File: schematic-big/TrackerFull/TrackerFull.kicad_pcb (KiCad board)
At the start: 2 copper layers, 43 x 61 mm, 50 parts, among them J1 SIM_Card, J2 Conn_01x05_Male, J7 Screw_Terminal_01x02, J8 USB_B_Mini, Q1 IRLML5203, Q2 IRLML0030, Q3 IRLML0030, U1 U.FL, U2 LIS3DSH, U3 MCP73831-2-OT, U4 LM350_TO220, U6 ATtiny85-20SU, U7 MCP1700-2502E_SOT23

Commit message: schematic fixes
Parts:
- C4, U7: moved to B.Cu
- R10, R11, R9: value 140 -> 125
- moved Q3 41.3 mm to (125.4, 101.8)
- moved U7 36.4 mm to (109.5, 90.7), turned to 180 degrees
- moved C4 31.8 mm to (106.4, 94.3), turned to 90 degrees
- moved C14 13.8 mm to (94.3, 41.5)
- moved D1 13.8 mm to (95.4, 44.6)
- moved R1 13.8 mm to (94.8, 48.4)
- moved R2 13.8 mm to (93.0, 48.4)
- moved U4 13.8 mm to (90.2, 47.7)
- moved L1 7.12 mm to (119.1, 60.3)
- moved C15 4.16 mm to (117.6, 55.2)
- moved LED1 2.60 mm to (91.4, 87.0)
- moved R10 2.60 mm to (92.0, 81.6)
- moved R11 2.60 mm to (95.5, 88.9)
- moved R9 2.60 mm to (95.5, 84.8)
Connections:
- LED1 pad 4: /VBAT -> /2.2V
- LED1 pad 5: /VBAT -> /2.2V
- LED1 pad 6: /VBAT -> /2.2V
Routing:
- net /2.2V: track 0.00 -> 24.4 mm, vias 0 -> 3
- net /VBAT: track 50.7 -> 34.9 mm

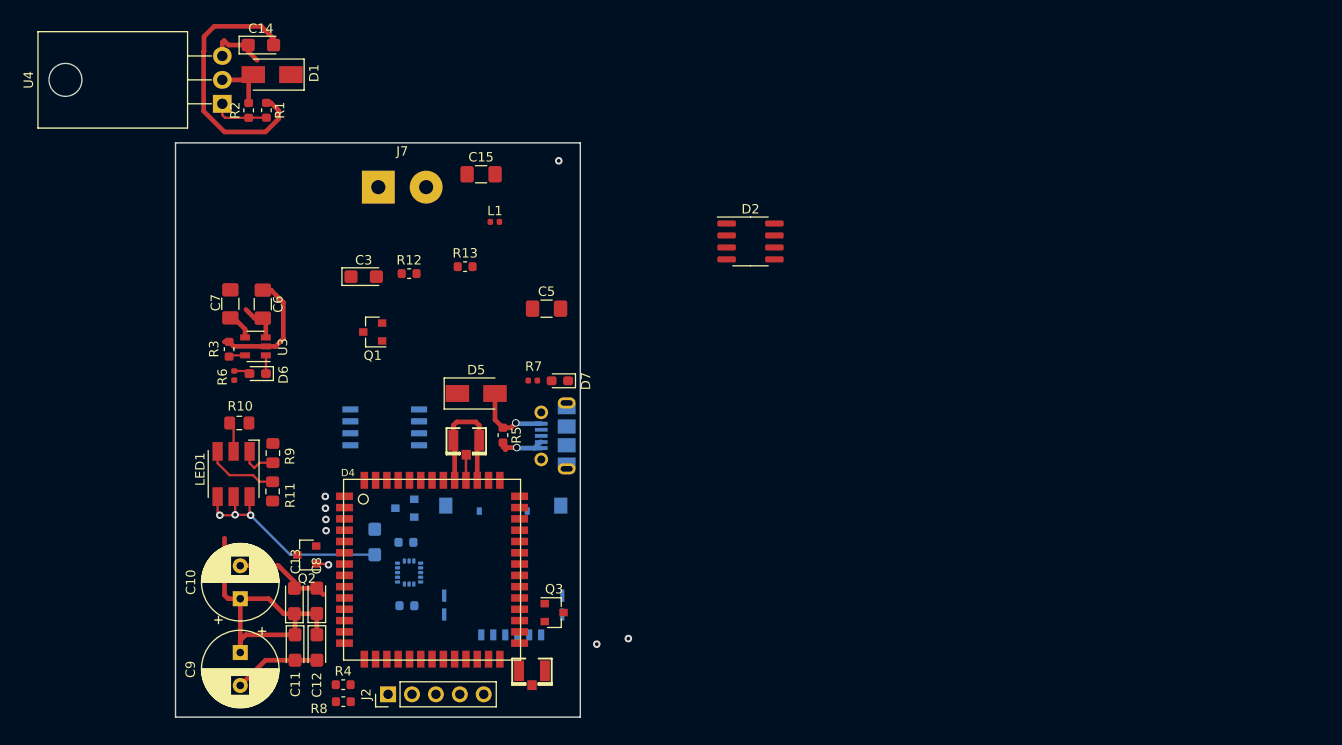
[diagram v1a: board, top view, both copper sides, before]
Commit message: schematic update
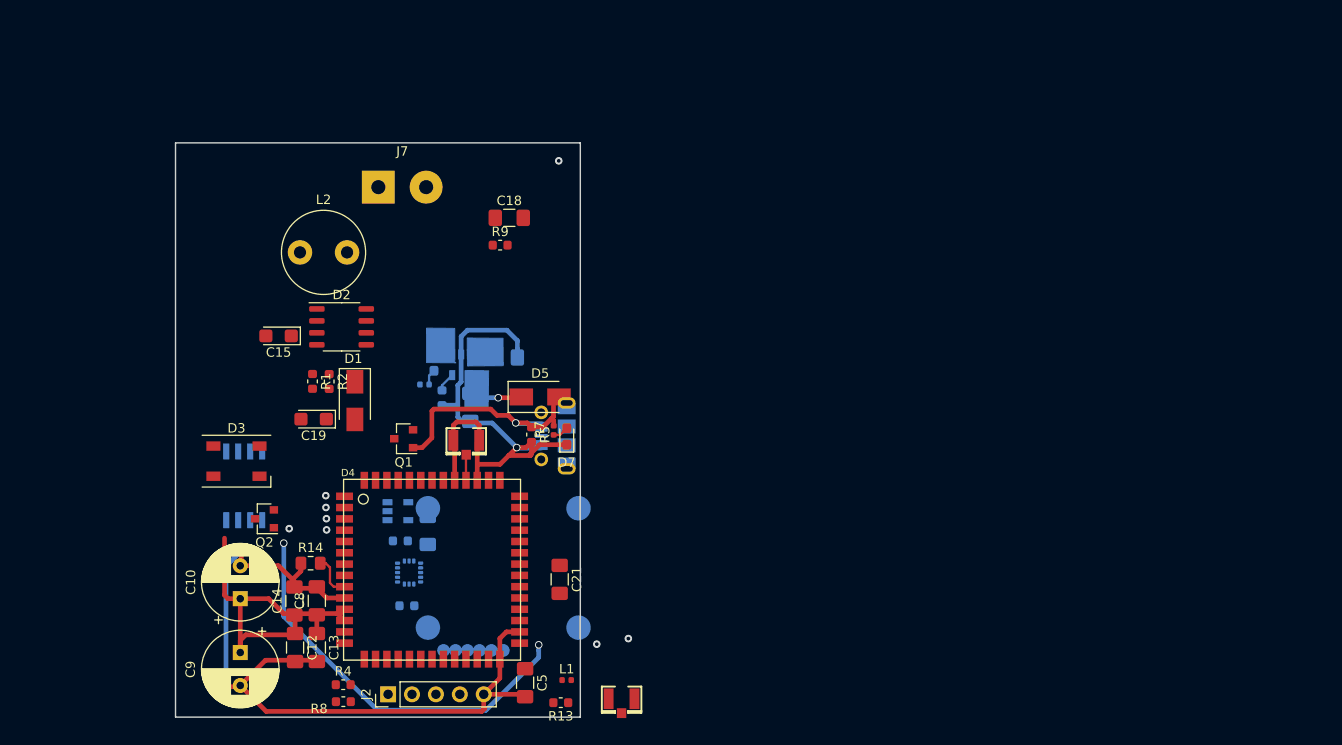
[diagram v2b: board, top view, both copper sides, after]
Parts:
- removed the C14 at (94.3, 41.5)
- removed C3, C4: 10uF, Capacitor_Tantalum_SMD:CP_EIA-3216-18_Kemet-A
- removed LED1: TO-5050BC-MRPBFGF, LED_SMD:LED_RGB_5050-6
- removed Q3: IRLML0030, Package_TO_SOT_SMD:SOT-23
- removed R10, R11: 125, Resistor_SMD:R_0805_2012Metric_Pad1.15x1.40mm_HandSolder
- removed R12: 100K, Resistor_SMD:R_0603_1608Metric
- removed U4: LM350_TO220, Package_TO_SOT_THT:TO-220-3_Horizontal_TabDown
- removed U7: MCP1700-2502E_SOT23, Package_TO_SOT_SMD:SOT-23
- added C18: 10uF, Capacitor_SMD:C_1206_3216Metric_Pad1.42x1.75mm_HandSolder, F.Cu at (120.6, 59.8)
- added C19: 22uF, Capacitor_Tantalum_SMD:CP_EIA-3216-18_Kemet-A, F.Cu at (99.9, 81.2)
- added C20: 4.7u, Capacitor_SMD:C_1206_3216Metric_Pad1.42x1.75mm_HandSolder, B.Cu at (112.0, 93.0)
- added C21: 4.7uF, Capacitor_SMD:C_1206_3216Metric_Pad1.42x1.75mm_HandSolder, F.Cu at (126.0, 98.2)
- added D3: SK6812, LED_SMD:LED_SK6812_PLCC4_5.0x5.0mm_P3.2mm, F.Cu at (91.7, 85.7)
- added L2: SRR0604-3R3ML, Inductor_THT:L_Radial_D8.7mm_P5.00mm_Fastron_07HCP, F.Cu at (98.4, 63.5)
- added R14: 10K, Resistor_SMD:R_0805_2012Metric_Pad1.15x1.40mm_HandSolder, F.Cu at (99.5, 96.5)
- added U5: LP2985-3.3, Package_TO_SOT_SMD:SOT-23-5, B.Cu at (108.8, 91.0)
- C12: renamed from C11; footprint Capacitor_Tantalum_SMD:CP_EIA-3216-18_Kemet-A -> Capacitor_SMD:C_1206_3216Metric_Pad1.42x1.75mm_HandSolder
- C13: renamed from C12; footprint Capacitor_Tantalum_SMD:CP_EIA-3216-18_Kemet-A -> Capacitor_SMD:C_1206_3216Metric_Pad1.42x1.75mm_HandSolder
- C14: renamed from C13; footprint Capacitor_Tantalum_SMD:CP_EIA-3216-18_Kemet-A -> Capacitor_SMD:C_1206_3216Metric_Pad1.42x1.75mm_HandSolder
- C15: value 4.7uF -> 10uF; footprint Capacitor_SMD:C_1206_3216Metric_Pad1.42x1.75mm_HandSolder -> Capacitor_Tantalum_SMD:CP_EIA-3216-18_Kemet-A
- C6, C7, D6, R3, R6, U3: moved to B.Cu
- C8: footprint Capacitor_Tantalum_SMD:CP_EIA-3216-18_Kemet-A -> Capacitor_SMD:C_1206_3216Metric_Pad1.42x1.75mm_HandSolder
- D2: footprint Package_SO:SOP-8_3.76x4.96mm_P1.27mm -> Package_SO:SOP-8_3.9x4.9mm_P1.27mm
- J1: footprint Connector_Card:microSIM_JAE_SF53S006VCBR2000 -> mailboxNotifier:SIM_SOCKET1
- R2: value 47000 -> 43000
- R9: value 125 -> 10000; footprint Resistor_SMD:R_0805_2012Metric_Pad1.15x1.40mm_HandSolder -> Resistor_SMD:R_0603_1608Metric
- moved L1 49.3 mm to (126.7, 108.9)
- moved R13 47.4 mm to (126.1, 111.3), turned to 180 degrees
- moved D2 44.4 mm to (102.8, 71.4)
- moved C5 39.8 mm to (122.3, 109.2), turned to 270 degrees
- moved D1 35.7 mm to (104.2, 79.2), turned to 270 degrees
- moved R9 32.7 mm to (119.7, 62.7), turned to 0 degrees
- moved R2 30.0 mm to (101.5, 77.2), turned to 270 degrees
- moved R1 29.2 mm to (99.7, 77.2)
- moved C6 27.8 mm to (116.5, 80.0), turned to 90 degrees
- moved C15 27.5 mm to (96.1, 72.4), turned to 180 degrees
- moved C7 26.2 mm to (120.0, 74.7), turned to 0 degrees
- moved R3 23.2 mm to (113.5, 78.9), turned to 90 degrees
- moved U3 21.9 mm to (115.5, 75.4), turned to 270 degrees
- moved R6 20.2 mm to (111.6, 77.5), turned to 0 degrees
- moved D6 18.8 mm to (112.6, 75.2), turned to 270 degrees
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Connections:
- C1 pad 2: /2.2V -> Net-(C1-Pad2)
- C15 pad 1: Net-(C15-Pad1) -> /CHARGER_VDD
- C2 pad 2: /2.2V -> Net-(C1-Pad2)
- C5 pad 1: Net-(C5-Pad1) -> /VBAT
- D1 pad 2: Net-(D1-Pad2) -> Net-(C19-Pad1)
- D2 pad 1: (no net) -> GNDREF
- D2 pad 2: (no net) -> /CHARGER_VDD
- D2 pad 3: (no net) -> GNDREF
- D2 pad 4: (no net) -> Net-(D2-Pad4)
- D2 pad 5: (no net) -> Net-(D2-Pad5)
- D2 pad 6: (no net) -> /CHARGER_VDD
- D2 pad 7: (no net) -> Net-(D2-Pad7)
- D2 pad 8: (no net) -> Net-(D2-Pad7)
- D4 pad 19: (no net) -> /ACCEL_SDO
- D4 pad 20: (no net) -> /ACCEL_CS
- D4 pad 3: /ACCEL_SDO -> (no net)
- D4 pad 30: Net-(D4-Pad30) -> (no net)
- D4 pad 31: Net-(D4-Pad31) -> (no net)
- D4 pad 32: /GPS_CTRL -> (no net)
- D4 pad 39: /SIM_IO -> (no net)
- D4 pad 4: /ACCEL_CS -> (no net)
- D4 pad 40: /VSIM -> (no net)
- D4 pad 41: /SIM_CLK -> (no net)
- D4 pad 42: /SIM_RST -> (no net)
- D4 pad 51: (no net) -> /ACCEL_INT1
- D4 pad 52: (no net) -> /ACCEL_INT2
- D4 pad 6: Net-(D4-Pad6) -> (no net)
- D4 pad 7: Net-(D4-Pad7) -> /IO9
- D4 pad 8: Net-(D4-Pad8) -> /IO8
- D4 pad 9: GNDREF -> Net-(D4-Pad9)
- R1 pad 1: GNDREF -> Net-(D2-Pad4)
- R1 pad 2: Net-(R1-Pad2) -> GNDREF
- R13 pad 1: Net-(C5-Pad1) -> /VBAT
- R13 pad 2: Net-(C15-Pad1) -> Net-(C21-Pad1)
- R2 pad 1: Net-(R1-Pad2) -> BAT_IN
- R2 pad 2: Net-(D1-Pad2) -> Net-(D2-Pad4)
- R9 pad 1: Net-(LED1-Pad1) -> Net-(D2-Pad5)
- R9 pad 2: Net-(D4-Pad8) -> Net-(C18-Pad2)
- U2 pad 1: /2.2V -> Net-(C1-Pad2)
- U2 pad 14: /2.2V -> Net-(C1-Pad2)
- U2 pad 15: /2.2V -> Net-(C1-Pad2)
- U2 pad 9: (no net) -> /ACCEL_INT2
- U6 pad 1: (no net) -> /LED_CTL
- U6 pad 2: Net-(D4-Pad31) -> /ACCEL_INT1
- U6 pad 3: (no net) -> /PWR_CTRL
- U6 pad 5: /ACCEL_INT1 -> /IO8
- U6 pad 6: /PWR_CTRL -> (no net)
- U6 pad 7: Net-(D4-Pad30) -> /IO9
- U6 pad 8: /2.2V -> BAT_IN
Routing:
- net GNDREF: track 82.8 -> 144.6 mm, vias 2 -> 4
- net /VBAT: track 34.9 -> 81.7 mm, vias 0 -> 2
- net /2.2V: track 24.4 -> 0.00 mm, vias 3 -> 0
- net +5V: track 8.30 -> 25.6 mm
- net Net-(LED1-Pad3): track 7.90 -> 0.00 mm
- net Net-(D1-Pad2): track 6.74 -> 0.00 mm
- net Net-(R1-Pad2): track 6.01 -> 0.00 mm
- net Net-(D4-Pad9): track 0.00 -> 4.57 mm
- net Net-(LED1-Pad1): track 4.15 -> 0.00 mm
- net Net-(LED1-Pad2): track 3.38 -> 0.00 mm
- net /V_BAT: track 4.36 -> 2.19 mm
- net Net-(D7-Pad2): track 0.00 -> 1.68 mm
- net /CHARGER_VDD: track 9.12 -> 7.59 mm, vias 0 -> 1
- net /PWR_CTRL: track 1.35 -> 0.00 mm
- net Net-(D3-Pad2): vias 0 -> 1
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
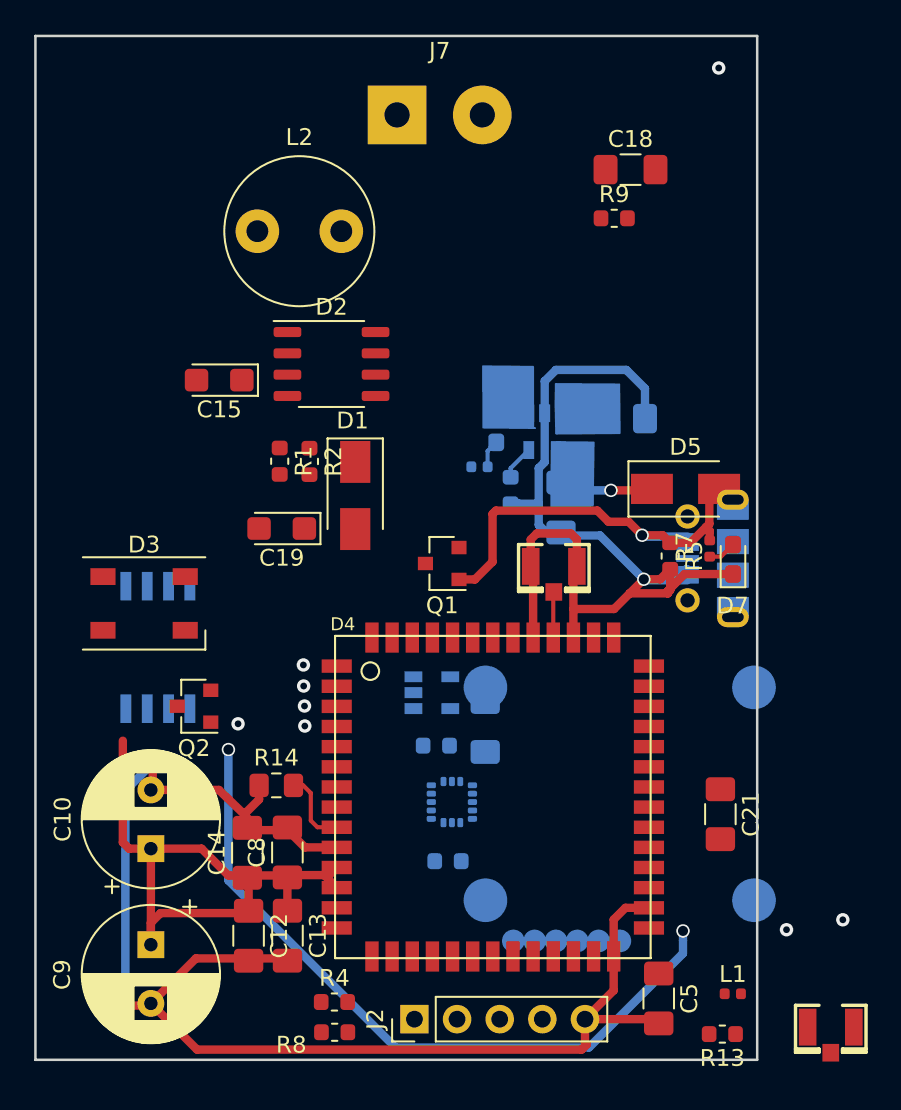
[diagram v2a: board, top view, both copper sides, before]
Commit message: schematic update
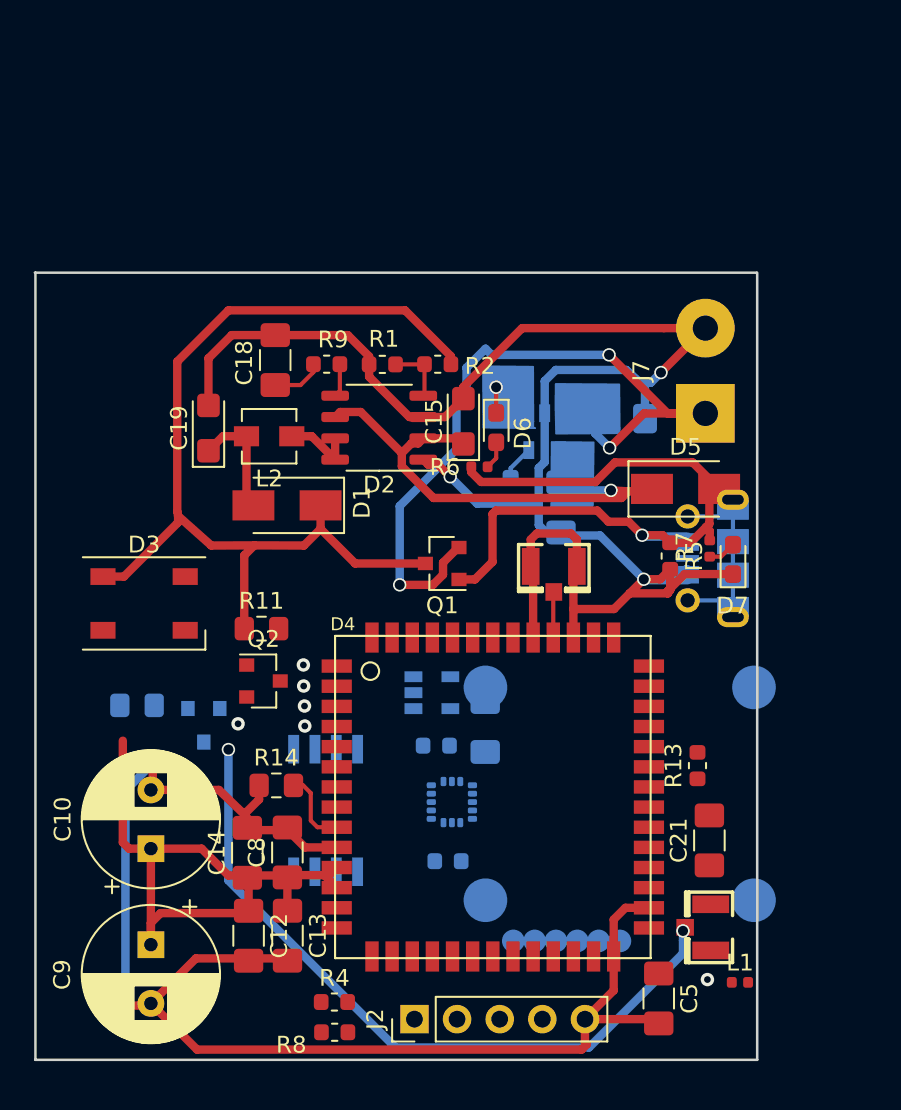
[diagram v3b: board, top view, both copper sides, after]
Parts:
- added Q2: IRLML5203, Package_TO_SOT_SMD:SOT-23, F.Cu at (98.8, 90.3)
- added R10: 100K, Resistor_SMD:R_0805_2012Metric_Pad1.15x1.40mm_HandSolder, B.Cu at (91.2, 91.7)
- added R11: 100K, Resistor_SMD:R_0805_2012Metric_Pad1.15x1.40mm_HandSolder, F.Cu at (98.7, 87.2)
- D6, R6: moved to F.Cu
- J8: value USB_B_Mini -> USB_B_Micro
- L2: value SRR0604-3R3ML -> IHLP1212BZER2R2M11; footprint Inductor_THT:L_Radial_D8.7mm_P5.00mm_Fastron_07HCP -> Inductor_SMD:L_Vishay_IHLP-1212
- Q3: renamed from Q2; moved to B.Cu
- moved J7 25.6 mm to (125.1, 74.3), turned to 90 degrees
- moved C18 24.0 mm to (99.5, 71.2), turned to 270 degrees
- moved R9 19.2 mm to (102.5, 71.4), turned to 180 degrees
- moved R13 16.1 mm to (124.6, 95.3), turned to 90 degrees
- moved C15 14.8 mm to (110.7, 74.8), turned to 90 degrees
- moved U6 13.9 mm to (102.5, 98.0)
- moved L2 12.2 mm to (99.1, 75.7), turned to 180 degrees
- moved R2 9.59 mm to (109.2, 71.4), turned to 180 degrees
- moved U1 9.30 mm to (125.4, 105.0), turned to 180 degrees
- moved R1 8.41 mm to (105.9, 71.4), turned to 180 degrees
- moved C19 7.40 mm to (95.5, 75.2), turned to 90 degrees
- moved D2 4.74 mm to (105.7, 75.2), turned to 180 degrees
- moved D1 4.11 mm to (100.2, 79.8), turned to 180 degrees
- moved C21 1.69 mm to (125.3, 99.8), turned to 90 degrees
- moved Q3 1.28 mm to (95.2, 92.9), turned to 270 degrees
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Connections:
- C19 pad 1: Net-(C19-Pad1) -> /APW_OUT
- D1 pad 2: Net-(C19-Pad1) -> /APW_OUT
- D2 pad 7: Net-(D2-Pad7) -> /LX
- D2 pad 8: Net-(D2-Pad7) -> /LX
- L2 pad 1: (no net) -> /LX
- L2 pad 2: (no net) -> /APW_OUT
- Q3 pad 2: BAT_IN -> GNDREF
- Q3 pad 3: /VBAT -> Net-(Q2-Pad1)
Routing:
- net BAT_IN: track 0.00 -> 57.9 mm
- net GNDREF: track 144.6 -> 195.0 mm, vias 4 -> 6
- net /V_BAT: track 2.19 -> 46.6 mm, vias 0 -> 3
- net /VBAT: track 81.7 -> 39.1 mm, vias 2 -> 0
- net /GPS_RF: track 0.00 -> 42.7 mm, vias 0 -> 2
- net /CHARGER_VDD: track 7.59 -> 32.1 mm
- net +5V: track 25.6 -> 41.8 mm
- net Net-(J8-Pad6): track 0.00 -> 12.9 mm
- net /APW_OUT: track 0.00 -> 6.91 mm
- net /LX: track 0.00 -> 4.43 mm
- net Net-(D2-Pad4): track 0.00 -> 3.64 mm
- net Net-(C18-Pad2): track 0.00 -> 3.07 mm
- net Net-(D2-Pad5): track 0.00 -> 2.00 mm
- net /CHARGER_STAT: track 1.94 -> 3.48 mm, vias 0 -> 1
- net (no net): vias 3 -> 1
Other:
- board size 43 x 61 mm -> 43 x 46.9 mm
